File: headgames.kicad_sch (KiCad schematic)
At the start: 44 parts, among them J1 ELECTRODES, J2 9V BATTERY IN, U1 LM324N INVENTORY, U2 LM386, U3 LM358N INVENTORY

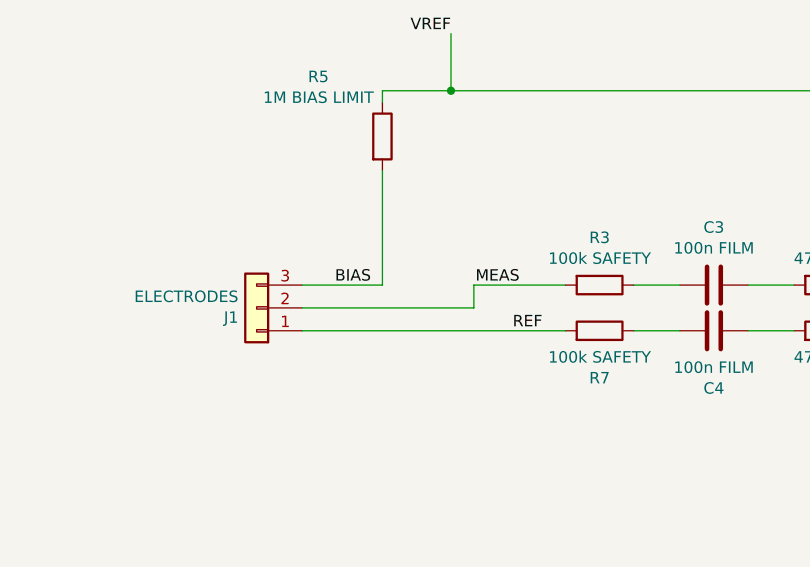
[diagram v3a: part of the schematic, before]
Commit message: Add independent current limiting at every electrode connection
Place a second physical series resistor immediately after each J1 electrode pin so a single resistor short cannot entirely remove the intended current limiting. MEAS and REF now each use two 100 kohm safety resistors for a nominal 45 microamp 9 V upper bound; BIAS uses two 1 Mohm resistors for a nominal 4.5 microamp upper bound.

Keep the connector-side nets deliberately limited to J1 and the outer resistor, then join each outer resistor to the existing inner limiter on a separate circuit-side net. This makes the no-bypass invariant explicit in the native netlist rather than relying on annotations.

Extend manage.py to verify the exact two-resistor topology and nominal current bounds for all three electrode paths. Update the project architecture and README while reiterating that redundant resistors do not replace isolated battery-only operation.

Verified with python3 manage.py test, including native KiCad netlist assertions and zero-violation ERC, plus git diff --check.
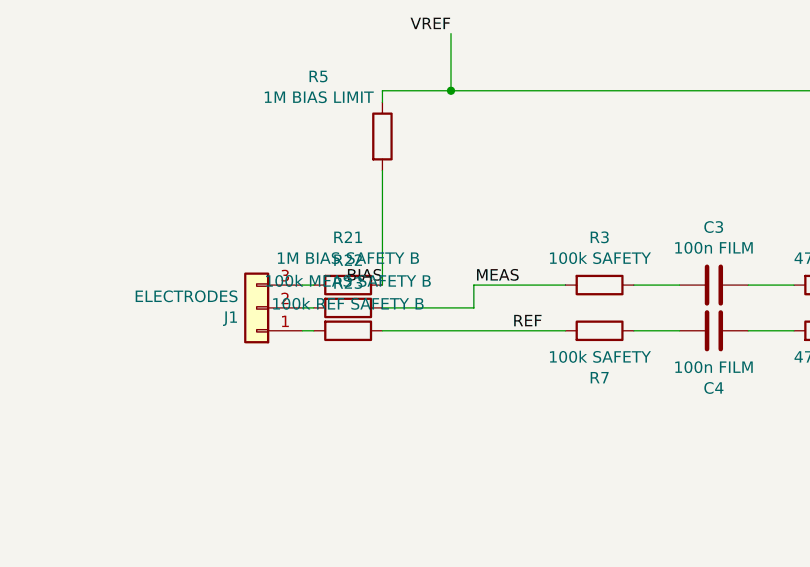
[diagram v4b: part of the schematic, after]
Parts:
- added R21: 1M BIAS SAFETY B, symbol Device:R
- added R22: 100k MEAS SAFETY B, symbol Device:R
- added R23: 100k REF SAFETY B, symbol Device:R
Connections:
- net BIAS: now also R21.1; no longer J1.3 (Pin_3)
- net MEAS: now also R22.1; no longer J1.2 (Pin_2)
- net REF: now also R23.1; no longer J1.1 (Pin_1)
- new net: J1.1 (Pin_1), R23.2
- new net: J1.2 (Pin_2), R22.2
- new net: J1.3 (Pin_3), R21.2
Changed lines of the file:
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@@
 	(wire
 		(pts
-			(xy 66.04 146.05) (xy 57.15 146.05)
-		)
-		(stroke
-			(width 0)
-			(type default)
-		)
-	)
-	(wire
-		(pts
-			(xy 57.15 148.59) (xy 76.2 148.59)
-		)
-		(stroke
-			(width 0)
-			(type default)
-		)
-	)
-	(wire
-		(pts
 			(xy 241.3 58.42) (xy 241.3 71.12)
 		)
@@
 	(wire
 		(pts
-			(xy 57.15 151.13) (xy 86.36 151.13)
-		)
-		(stroke
-			(width 0)
-			(type default)
-		)
-	)
-	(wire
-		(pts
 			(xy 228.6 38.1) (xy 238.76 38.1)
 		)
@@
 		(stroke (width 0) (type default))
 	)
+	(wire
+		(pts (xy 57.15 146.05) (xy 58.42 146.05))
+		(stroke (width 0) (type default))
+	)
+	(wire
+		(pts (xy 57.15 148.59) (xy 58.42 148.59))
+		(stroke (width 0) (type default))
+	)
+	(wire
+		(pts (xy 66.04 148.59) (xy 76.2 148.59))
+		(stroke (width 0) (type default))
+	)
+	(wire
+		(pts (xy 57.15 151.13) (xy 58.42 151.13))
+		(stroke (width 0) (type default))
+	)
+	(wire
+		(pts (xy 66.04 151.13) (xy 86.36 151.13))
+		(stroke (width 0) (type default))
+	)
 	(label "ALPHA"
 		(at 252.73 182.88 0)
@@
 	)
 	(label "BIAS"
-		(at 64.77 146.05 180)
+		(at 66.04 146.05 180)
 		(effects
 			(font
@@
 		(instances (project "headgames" (path "/16bca6b0-2f64-4676-a185-d512cb0de7e5" (reference "C17") (unit 1))))
 	)
+	(symbol
+		(lib_id "Device:R")
+		(at 62.23 146.05 270)
+		(unit 1)
+		(exclude_from_sim no)
+		(in_bom yes)
+		(on_board yes)
+		(dnp no)
+		(property "Reference" "R21" (at 62.23 140.7922 90) (effects (font (size 1.27 1.27))))
+		(property "Value" "1M BIAS SAFETY B" (at 62.23 143.1036 90) (effects (font (size 1.27 1.27))))
+		(property "Footprint" "" (at 62.23 146.05 0) (effects (font (size 1.27 1.27)) (hide yes)))
+		(property "Datasheet" "" (at 62.23 146.05 0) (effects (font (size 1.27 1.27)) (hide yes)))
+		(property "Description" "Independent electrode current-limiting resistor" (at 62.23 146.05 0) (effects (font (size 1.27 1.27)) (hide yes)))
+		(pin "1")
+		(pin "2")
+		(instances (project "headgames" (path "/16bca6b0-2f64-4676-a185-d512cb0de7e5" (reference "R21") (unit 1))))
+	)
+	(symbol
+		(lib_id "Device:R")
+		(at 62.23 148.59 270)
+		(unit 1)
+		(exclude_from_sim no)
+		(in_bom yes)
+		(on_board yes)
+		(dnp no)
+		(property "Reference" "R22" (at 62.23 143.3322 90) (effects (font (size 1.27 1.27))))
+		(property "Value" "100k MEAS SAFETY B" (at 62.23 145.6436 90) (effects (font (size 1.27 1.27))))
+		(property "Footprint" "" (at 62.23 148.59 0) (effects (font (size 1.27 1.27)) (hide yes)))
+		(property "Datasheet" "" (at 62.23 148.59 0) (effects (font (size 1.27 1.27)) (hide yes)))
+		(property "Description" "Independent electrode current-limiting resistor" (at 62.23 148.59 0) (effects (font (size 1.27 1.27)) (hide yes)))
+		(pin "1")
+		(pin "2")
+		(instances (project "headgames" (path "/16bca6b0-2f64-4676-a185-d512cb0de7e5" (reference "R22") (unit 1))))
+	)
+	(symbol
+		(lib_id "Device:R")
+		(at 62.23 151.13 270)
+		(unit 1)
+		(exclude_from_sim no)
+		(in_bom yes)
+		(on_board yes)
+		(dnp no)
+		(property "Reference" "R23" (at 62.23 145.8722 90) (effects (font (size 1.27 1.27))))
+		(property "Value" "100k REF SAFETY B" (at 62.23 148.18359999999998 90) (effects (font (size 1.27 1.27))))
+		(property "Footprint" "" (at 62.23 151.13 0) (effects (font (size 1.27 1.27)) (hide yes)))
+		(property "Datasheet" "" (at 62.23 151.13 0) (effects (font (size 1.27 1.27)) (hide yes)))
+		(property "Description" "Independent electrode current-limiting resistor" (at 62.23 151.13 0) (effects (font (size 1.27 1.27)) (hide yes)))
+		(pin "1")
+		(pin "2")
+		(instances (project "headgames" (path "/16bca6b0-2f64-4676-a185-d512cb0de7e5" (reference "R23") (unit 1))))
+	)
 	(sheet_instances

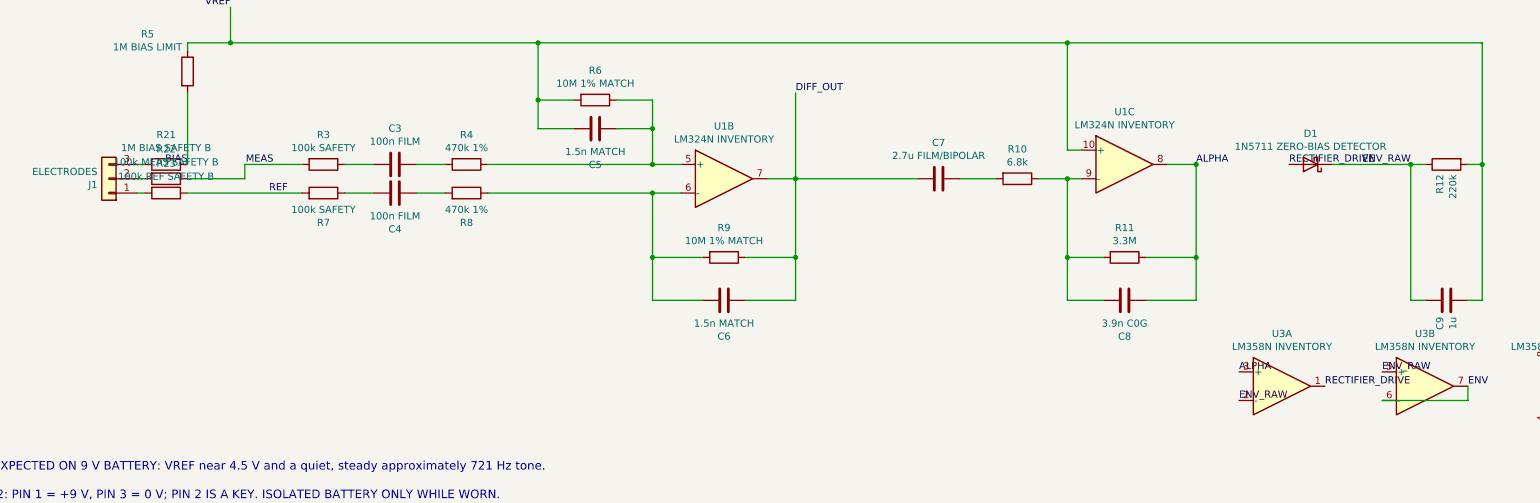
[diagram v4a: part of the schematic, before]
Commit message: Clarify the new detector and electrode safety annotations
Replace long internal detector net names with compact DRV and HOLD labels so the precision-feedback connections remain legible on the A3 sheet. Shorten the D1 display value while retaining the exact 1N5711 part identity in both the schematic value and automated invariant.

Keep the tightly spaced connector-side resistors identifiable by compact reference labels and add one authoritative callout stating their roles and values, rather than allowing three repeated long value strings to obscure the electrode wiring.

Verified the rendered schematic visually after native SVG export, then reran python3 manage.py test for connectivity and zero-violation ERC and checked whitespace with git diff --check.
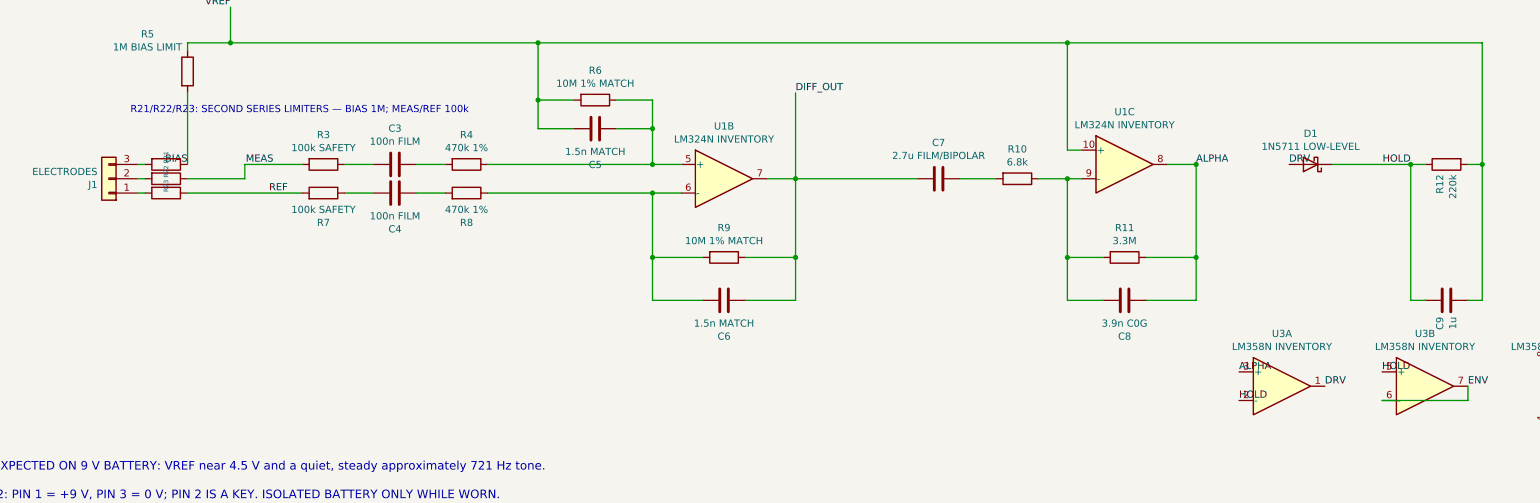
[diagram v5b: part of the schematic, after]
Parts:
- D1: value 1N5711 ZERO-BIAS DETECTOR -> 1N5711 LOW-LEVEL
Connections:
- net ENV_RAW renamed HOLD
- net RECTIFIER_DRIVE renamed DRV
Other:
- note added: "R21/R22/R23: SECOND SERIES LIMITERS — BIAS 1M; MEAS/REF 100k"
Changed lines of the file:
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@@
 		)
 	)
+	(text "R21/R22/R23: SECOND SERIES LIMITERS — BIAS 1M; MEAS/REF 100k"
+		(exclude_from_sim no)
+		(at 55.88 137.16 0)
+		(effects
+			(font (size 1.27 1.27))
+			(justify left bottom)
+		)
+	)
 	(junction
 		(at 231.14 107.95)
@@
 		)
 	)
-	(label "ENV_RAW"
+	(label "HOLD"
 		(at 252.73 187.96 0)
 		(effects
@@
 		)
 	)
-	(label "RECTIFIER_DRIVE"
+	(label "DRV"
 		(at 267.97 185.42 0)
 		(effects
@@
 		)
 	)
-	(label "RECTIFIER_DRIVE"
+	(label "DRV"
 		(at 261.62 146.05 0)
 		(effects
@@
 		)
 	)
-	(label "ENV_RAW"
+	(label "HOLD"
 		(at 278.13 182.88 0)
 		(effects
@@
 		)
 	)
-	(label "ENV_RAW"
+	(label "HOLD"
 		(at 283.21 146.05 180)
 		(effects
@@
 			)
 		)
-		(property "Value" "1N5711 ZERO-BIAS DETECTOR"
+		(property "Value" "1N5711 LOW-LEVEL"
 			(at 265.43 142.875 0)
 			(effects
@@
 		(on_board yes)
 		(dnp no)
-		(property "Reference" "R21" (at 62.23 140.7922 90) (effects (font (size 1.27 1.27))))
-		(property "Value" "1M BIAS SAFETY B" (at 62.23 143.1036 90) (effects (font (size 1.27 1.27))))
+		(property "Reference" "R21" (at 62.23 144.78 0) (effects (font (size 0.8 0.8))))
+		(property "Value" "1M BIAS SAFETY B" (at 62.23 146.05 0) (effects (font (size 1.27 1.27)) (hide yes)))
 		(property "Footprint" "" (at 62.23 146.05 0) (effects (font (size 1.27 1.27)) (hide yes)))
 		(property "Datasheet" "" (at 62.23 146.05 0) (effects (font (size 1.27 1.27)) (hide yes)))
@@
 		(on_board yes)
 		(dnp no)
-		(property "Reference" "R22" (at 62.23 143.3322 90) (effects (font (size 1.27 1.27))))
-		(property "Value" "100k MEAS SAFETY B" (at 62.23 145.6436 90) (effects (font (size 1.27 1.27))))
+		(property "Reference" "R22" (at 62.23 147.32 0) (effects (font (size 0.8 0.8))))
+		(property "Value" "100k MEAS SAFETY B" (at 62.23 148.59 0) (effects (font (size 1.27 1.27)) (hide yes)))
 		(property "Footprint" "" (at 62.23 148.59 0) (effects (font (size 1.27 1.27)) (hide yes)))
 		(property "Datasheet" "" (at 62.23 148.59 0) (effects (font (size 1.27 1.27)) (hide yes)))
@@
 		(on_board yes)
 		(dnp no)
-		(property "Reference" "R23" (at 62.23 145.8722 90) (effects (font (size 1.27 1.27))))
-		(property "Value" "100k REF SAFETY B" (at 62.23 148.18359999999998 90) (effects (font (size 1.27 1.27))))
+		(property "Reference" "R23" (at 62.23 149.86 0) (effects (font (size 0.8 0.8))))
+		(property "Value" "100k REF SAFETY B" (at 62.23 151.13 0) (effects (font (size 1.27 1.27)) (hide yes)))
 		(property "Footprint" "" (at 62.23 151.13 0) (effects (font (size 1.27 1.27)) (hide yes)))
 		(property "Datasheet" "" (at 62.23 151.13 0) (effects (font (size 1.27 1.27)) (hide yes)))

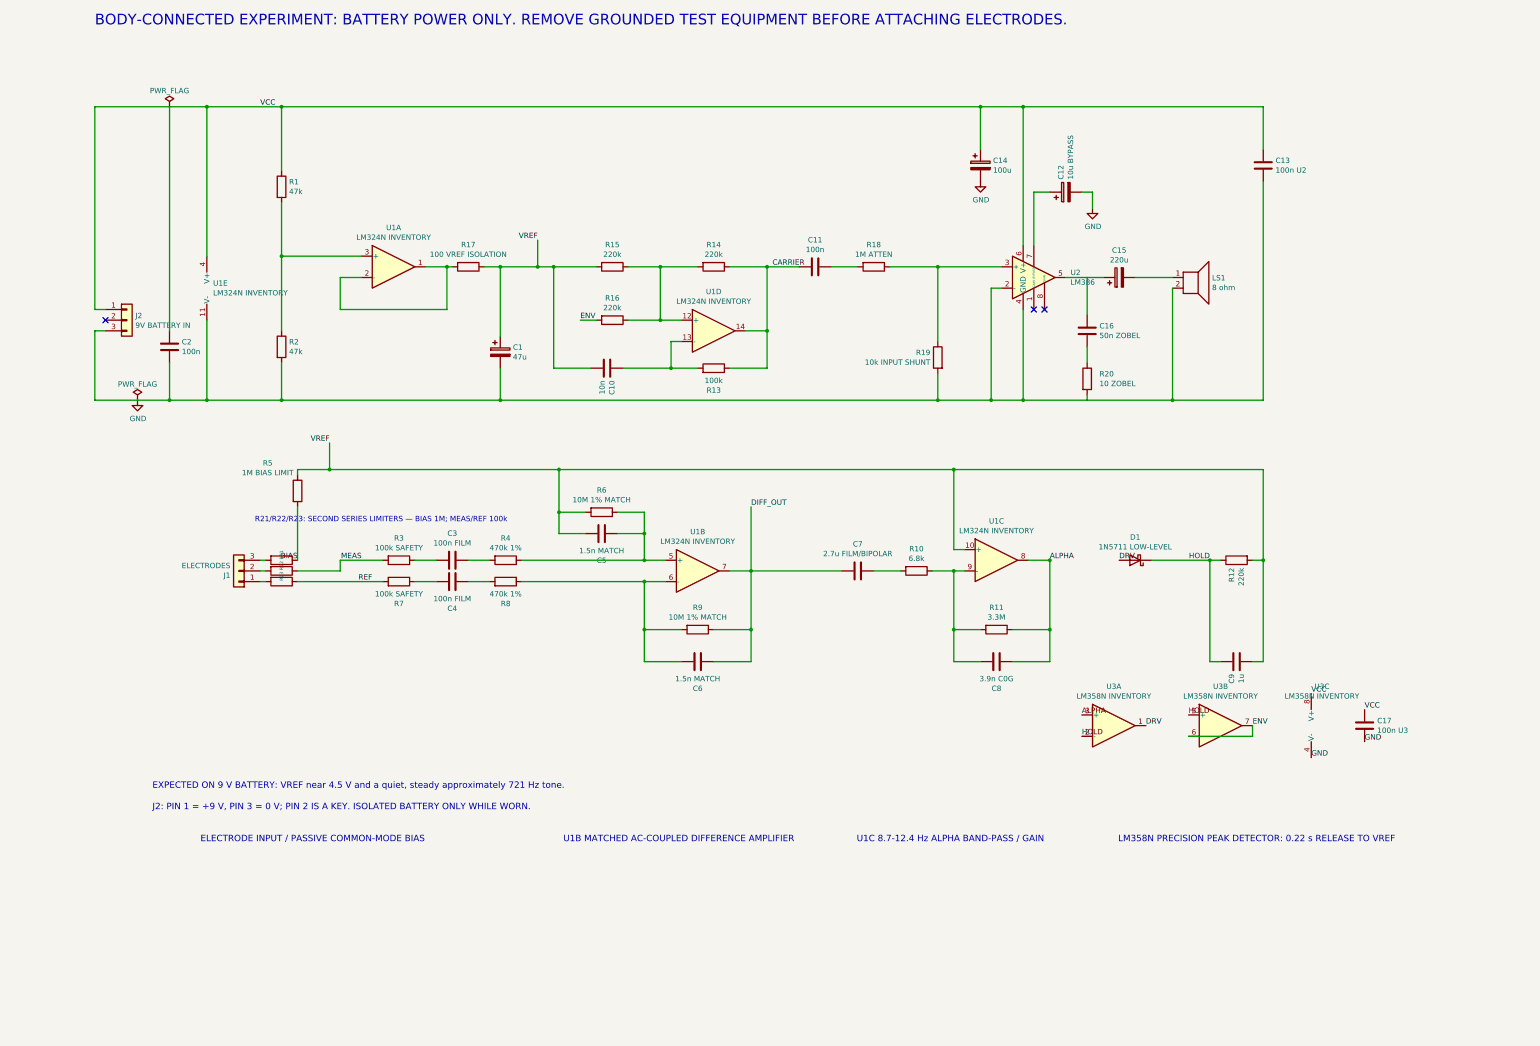
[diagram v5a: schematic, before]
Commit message: Add bounded alpha-band corner tuning
Introduce fixed-plus-trimmer resistance in both alpha filter corner networks so calibration cannot remove the stage's limiting resistance. The high-pass uses 6.2 kOhm fixed plus a 1 kOhm multiturn trim for an approximately 8.19-9.51 Hz range with the existing 2.7 uF capacitor. The low-pass uses 3 MOhm fixed plus a 500 kOhm multiturn trim for an approximately 11.66-13.60 Hz range with the existing 3.9 nF capacitor.

Represent each external three-terminal trimmer as a two-terminal rheostat in the authoritative schematic and add an explicit assembly instruction to strap the wiper to the used end terminal. This gives a defined failure tendency if wiper contact becomes intermittent while keeping potentiometers out of electrode safety and differential matching paths.

Update the durable Typer verification entrypoint for the schematic's current annotation, assert each trim remains in series with its fixed resistor, bound both achievable corner ranges so they cannot overlap, and require every resistor, trimmer, and capacitor to carry a nonempty value. Retain the existing connectivity, safety-current, detector, supply, audio-drive, stabilization, and full KiCad ERC checks.
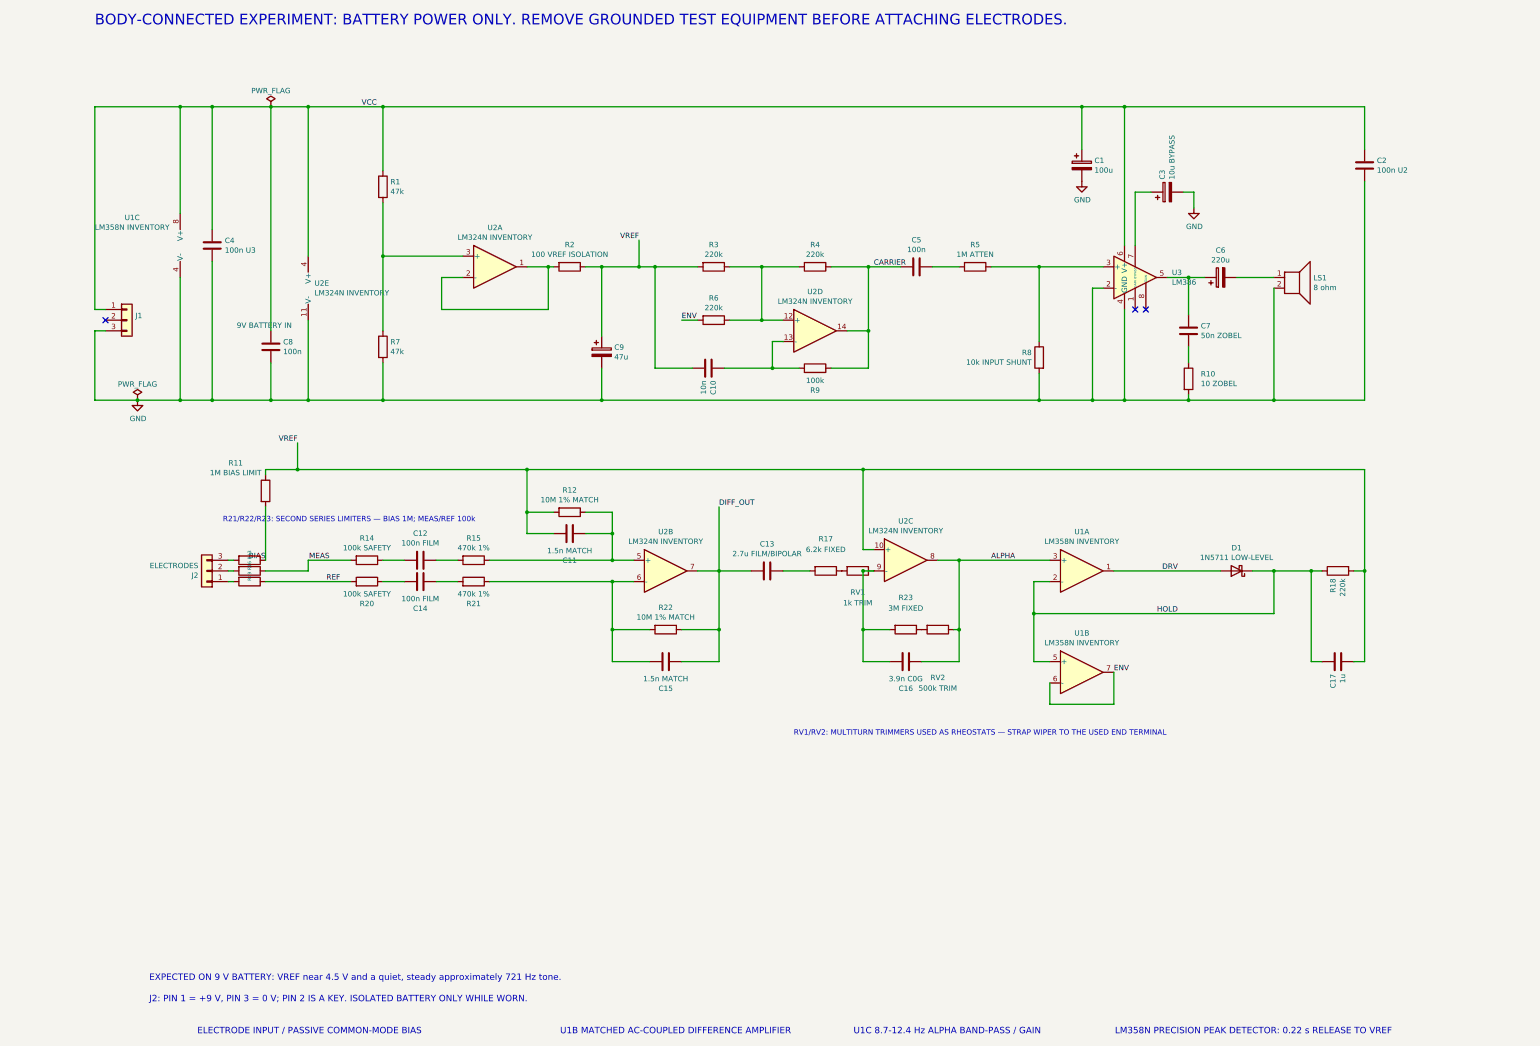
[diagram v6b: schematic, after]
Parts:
- added RV1: 1k TRIM, symbol Device:R
- added RV2: 500k TRIM, symbol Device:R
- R17: renamed from R10; value 6.8k -> 6.2k FIXED
- R23: renamed from R11; value 3.3M -> 3M FIXED
- renumbered C14 to C1, C5 to C11, C3 to C12, C7 to C13, C4 to C14, C6 to C15, C8 to C16, C9 to C17, C13 to C2, C12 to C3, C17 to C4, C11 to C5, C15 to C6, C16 to C7, C2 to C8, C1 to C9, J2 to J1, J1 to J2, R20 to R10, R5 to R11, R6 to R12, R21 to R13, R3 to R14, R4 to R15, R22 to R16, R12 to R18, R23 to R19, R17 to R2, R7 to R20, R8 to R21, R9 to R22, R15 to R3, R14 to R4, R18 to R5, R16 to R6, R2 to R7, R19 to R8, R13 to R9, U3 to U1, U1 to U2, U2 to U3
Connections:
- net ALPHA: now also RV2.1; no longer R23.1
- net at C16.2, R23.2, U2.9 (-): now also RV1.1; no longer R17.1
- new net: R17.1, RV1.2
- new net: R23.1, RV2.2
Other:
- note added: "RV1/RV2: MULTITURN TRIMMERS USED AS RHEOSTATS — STRAP WIPER TO THE USED END TERMINAL"
- moved on the sheet: C1, C10, C11, C12, C13, C14, C15, C16, C17, C2, C3, C4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
